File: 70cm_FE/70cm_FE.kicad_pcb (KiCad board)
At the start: 2 copper layers, 60 x 60 mm, 130 parts, among them J2 U.FL, J3 U.FL, J4 U.FL, Q1 2SC3356, Q2 2SC3356, Q3 2SC3356, U1 HT7533-1, U2 74HC14, U3 M68710L, U4 LM393

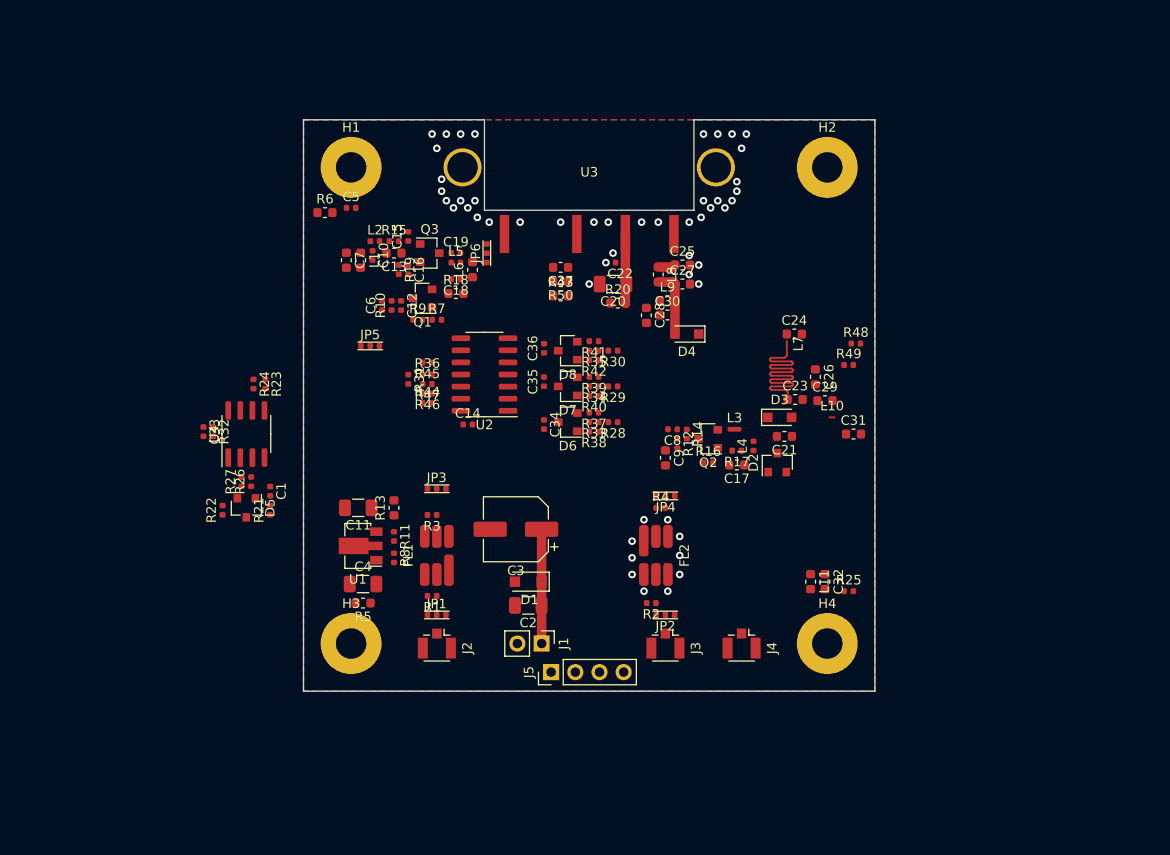
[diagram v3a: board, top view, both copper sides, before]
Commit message: Fix control signal polarities, draft more layout
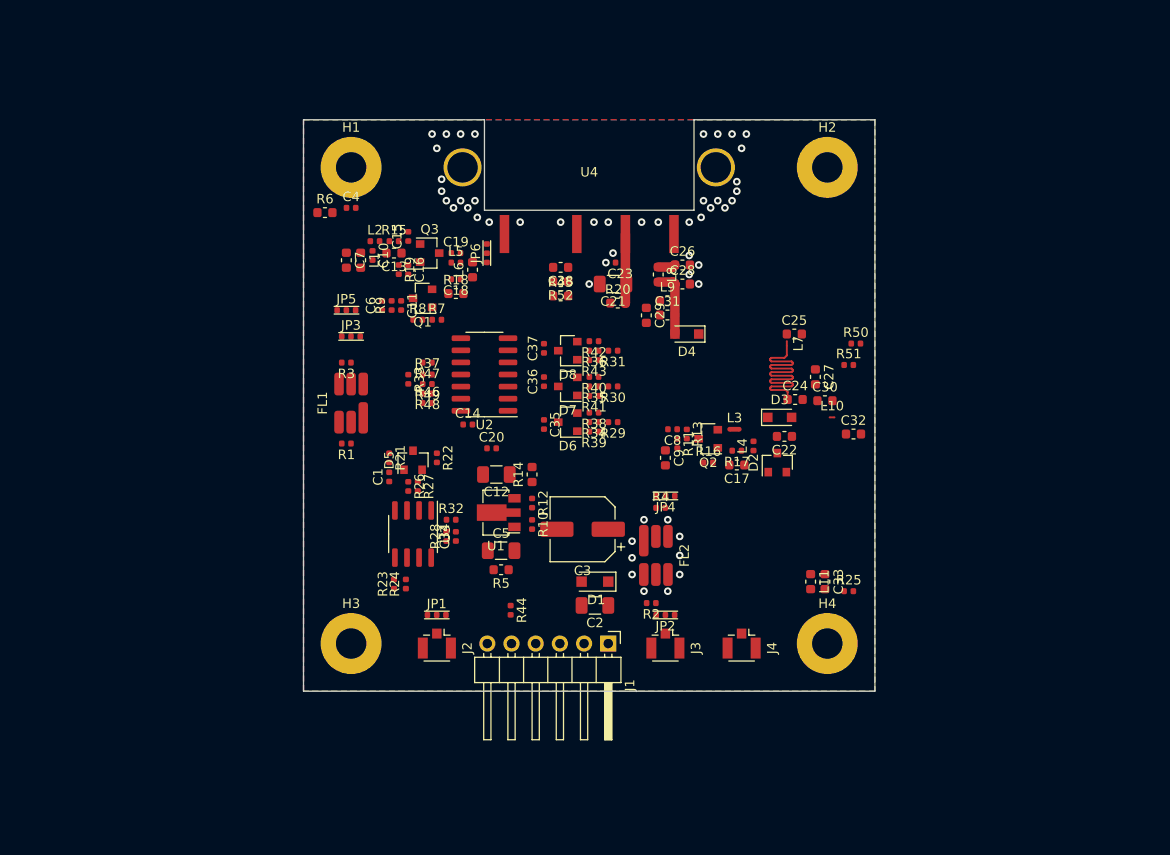
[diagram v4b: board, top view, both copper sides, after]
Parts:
- removed J5: ~, Connector_PinHeader_2.54mm:PinHeader_1x04_P2.54mm_Vertical
- added C20: 100n, Capacitor_SMD:C_0402_1005Metric, F.Cu at (114.8, 84.5)
- added R32: 100, Resistor_SMD:R_0402_1005Metric, F.Cu at (110.5, 92.0)
- added R44: 100, Resistor_SMD:R_0402_1005Metric, F.Cu at (116.8, 101.5)
- J1: footprint Connector_PinHeader_2.54mm:PinHeader_1x02_P2.54mm_Vertical -> Connector_PinHeader_2.54mm:PinHeader_1x06_P2.54mm_Horizontal
- R28: renamed from R32; value 100k -> 220k
- R34: renamed from R33; value 0 -> 220k
- R35: renamed from R34; value 0 -> 100k
- R39: renamed from R38; value DNP -> 0
- moved C34 28.7 mm to (111.0, 93.8), turned to 90 degrees
- moved R28 26.9 mm to (110.0, 93.8), turned to 90 degrees
- moved R24 26.4 mm to (105.8, 98.8), turned to 90 degrees
- moved R23 25.0 mm to (104.5, 98.8), turned to 90 degrees
- moved R22 23.2 mm to (109.0, 85.5), turned to 270 degrees
- moved U3 20.4 mm to (106.5, 93.5), turned to 270 degrees
- moved R27 18.5 mm to (107.0, 88.5), turned to 270 degrees
- moved FL1 18.4 mm to (100.0, 79.8)
- moved JP3 18.4 mm to (99.5, 72.8)
- moved R1 18.4 mm to (99.5, 84.0)
- moved R3 18.4 mm to (99.5, 75.5)
- moved D5 18.2 mm to (106.5, 85.8), turned to 90 degrees
- moved R26 16.5 mm to (106.0, 88.5), turned to 270 degrees
- moved C12 14.9 mm to (115.2, 87.2)
- moved C5 14.9 mm to (115.8, 95.2)
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- renumbered C12 to C11, C11 to C12, C20 to C21, C21 to C22, C22 to C23, C23 to C24, C24 to C25, C25 to C26, C26 to C27, C27 to C28, C28 to C29, C29 to C30, C30 to C31, C31 to C32, C32 to C33, C33 to C34, C34 to C35, C35 to C36, C36 to C37, C37 to C38, C5 to C4, C4 to C5, R8 to R10, R12 to R11, R11 to R12, R14 to R13, R13 to R14, R28 to R29, R29 to R30, R30 to R31, R31 to R33, R35 to R36, R36 to R37, R37 to R38, R39 to R40, R40 to R41, R41 to R42, R42 to R43, R43 to R45, R44 to R46, R45 to R47, R46 to R48, R47 to R49, R48 to R50, R49 to R51, R50 to R52, R9 to R8, R10 to R9, U4 to U3, U3 to U4
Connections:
- net /DET_IN+ renamed /DET_COMP+
- net /DET_IN- renamed /DET_COMP-
- R28 pad 2: /DET_timing -> /DET_COMPout
- R30 pad 1: /TX_ON -> /~TX_ON~
- U2 pad 8: /TX_detect -> /DET_OUT_
- U3 pad 1: /DET_timing -> /DET_COMPout
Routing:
- net /V_in: track 11.5 -> 0.00 mm

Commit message: Add overtemperature protection
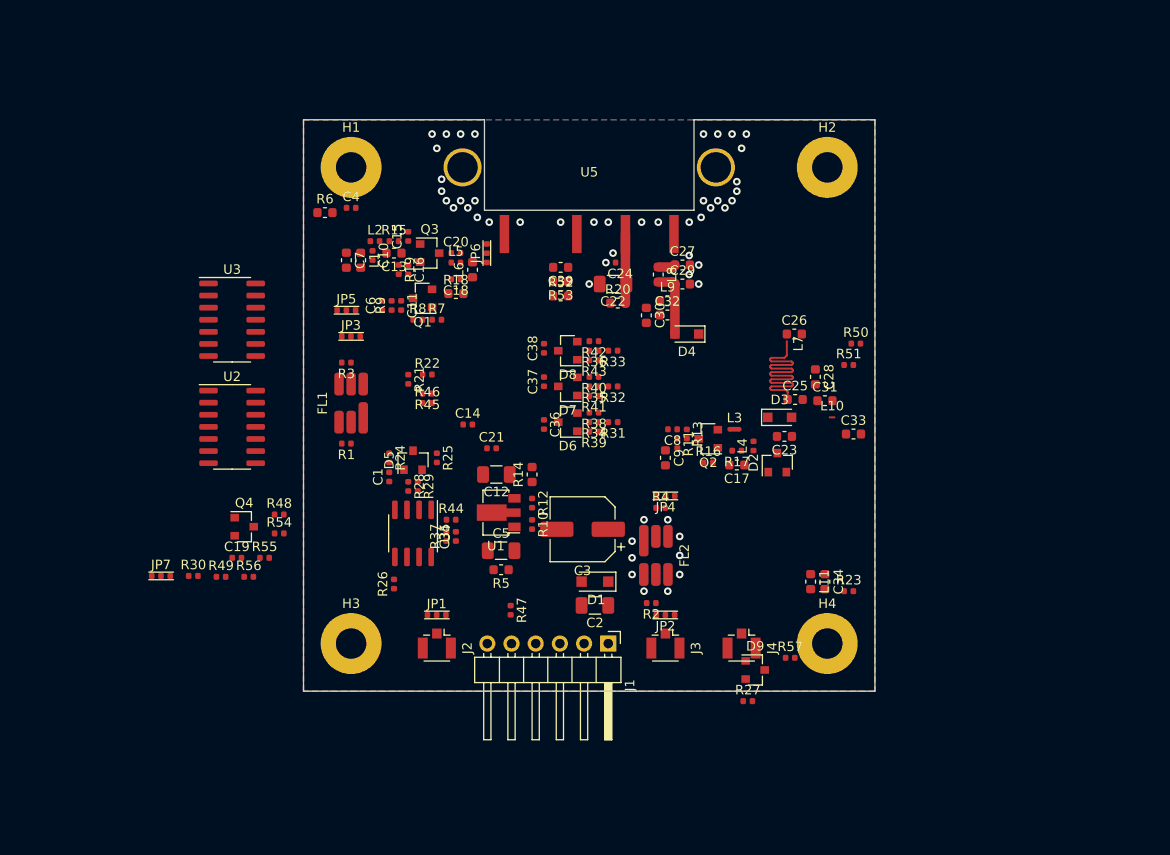
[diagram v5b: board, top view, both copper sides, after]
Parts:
- removed the R24 at (105.8, 98.8)
- removed the R47 at (108.0, 75.5)
- added C19: 100n, Capacitor_SMD:C_0402_1005Metric, F.Cu at (88.0, 96.0)
- added D9: BAV99, Package_TO_SOT_SMD:SOT-23, F.Cu at (142.4, 107.8)
- added JP7: ~, 70cm_FE:Jumper-3_0402, F.Cu at (79.5, 97.9)
- added Q4: 2N7002, Package_TO_SOT_SMD:SOT-23, F.Cu at (88.8, 92.7)
- added R27: 100k, Resistor_SMD:R_0402_1005Metric, F.Cu at (141.7, 111.0)
- added R30: 100k, Resistor_SMD:R_0402_1005Metric, F.Cu at (83.4, 97.9)
- added R48: 100, Resistor_SMD:R_0402_1005Metric, F.Cu at (92.5, 91.5)
- added R54: 1k, Resistor_SMD:R_0402_1005Metric, F.Cu at (92.5, 93.4)
- added R55: 1k, Resistor_SMD:R_0402_1005Metric, F.Cu at (90.9, 96.0)
- added R56: 1k, Resistor_SMD:R_0402_1005Metric, F.Cu at (89.2, 98.0)
- added R57: 10k, Resistor_SMD:R_0402_1005Metric, F.Cu at (146.1, 106.5)
- added U4: LM393, Package_SO:SOIC-8_3.9x4.9mm_P1.27mm, F.Cu at (106.5, 93.4)
- R49: value DNP -> 100k
- U3: value LM393 -> 74HC14; footprint Package_SO:SOIC-8_3.9x4.9mm_P1.27mm -> Package_SO:SOIC-14_3.9x8.7mm_P1.27mm
- moved R49 29.6 mm to (86.3, 98.0), turned to 0 degrees
- moved U3 29.4 mm to (87.5, 71.0), turned to 0 degrees
- moved U2 27.1 mm to (87.5, 82.2), turned to 0 degrees
- renumbered C19 to C20, C20 to C21, C21 to C22, C22 to C23, C23 to C24, C24 to C25, C25 to C26, C26 to C27, C27 to C28, C28 to C29, C29 to C30, C30 to C31, C31 to C32, C32 to C33, C33 to C34, C34 to C35, C35 to C36, C36 to C37, C37 to C38, C38 to C39, R33 to R21, R37 to R22, R25 to R23, R21 to R24, R22 to R25, R23 to R26, R26 to R28, R27 to R29, R29 to R31, R30 to R32, R31 to R33, R28 to R37, R32 to R44, R48 to R45, R44 to R47, R45 to R52, R52 to R53, U4 to U5
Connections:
- R22 pad 2: Net-(R37-Pad2) -> Net-(R22-Pad2)
- R26 pad 1: GND -> /VDD
- R26 pad 2: Net-(R23-Pad2) -> /TempSensor
- R32 pad 1: /~TX_ON~ -> /TX_ON
- R33 pad 1: /~TX_ON~ -> /TX_ON
- R45 pad 1: Net-(R48-Pad1) -> Net-(R45-Pad1)
- R45 pad 2: /TX_ON -> Net-(R45-Pad2)
- R46 pad 1: Net-(R46-Pad1) -> Net-(R45-Pad1)
- R46 pad 2: /~TX_ON~ -> Net-(R46-Pad2)
- R49 pad 1: Net-(R48-Pad1) -> /VDD
- R49 pad 2: /~TX_ON~ -> /~PA_EN_Protected~
- R51 pad 1: Net-(R50-Pad1) -> Net-(R51-Pad1)
- R52 pad 1: /PA_EN -> Net-(R52-Pad1)
- U2 pad 1: /~LNA_EN_SEQ~ -> /~PIN_EN_SEQ~
- U2 pad 10: Net-(R46-Pad1) -> /~PA_EN_1~
- U2 pad 11: Net-(R37-Pad2) -> /~PA_EN_SEQ~
- U2 pad 12: Net-(R48-Pad1) -> Net-(R52-Pad1)
- U2 pad 13: Net-(R46-Pad1) -> /~PA_EN_Protected~
- U2 pad 2: /LNA_EN -> Net-(R45-Pad1)
- U2 pad 3: /~PIN_EN_SEQ~ -> Net-(R45-Pad2)
- U2 pad 5: /~PA_EN_SEQ~ -> Net-(R46-Pad2)
- U2 pad 6: /PA_EN -> Net-(R51-Pad1)
- U2 pad 8: /DET_OUT_ -> /LNA_EN
- U2 pad 9: /DET_timing -> /~LNA_EN_SEQ~
- U3 pad 1: /DET_COMPout -> Net-(R22-Pad2)
- U3 pad 2: /DET_COMP- -> Net-(JP7-Pad3)
- U3 pad 3: /DET_COMP+ -> Net-(JP7-Pad3)
- U3 pad 4: GND -> Net-(JP7-Pad1)
- U3 pad 5: Net-(R23-Pad2) -> /DET_timing
- U3 pad 6: Net-(R24-Pad2) -> /DET_OUT_
- U3 pad 7: Net-(U3-Pad7) -> GND
- U3 pad 8: /VDD -> Net-(U3-Pad8)

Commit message: Change order of inverters for simpler layout
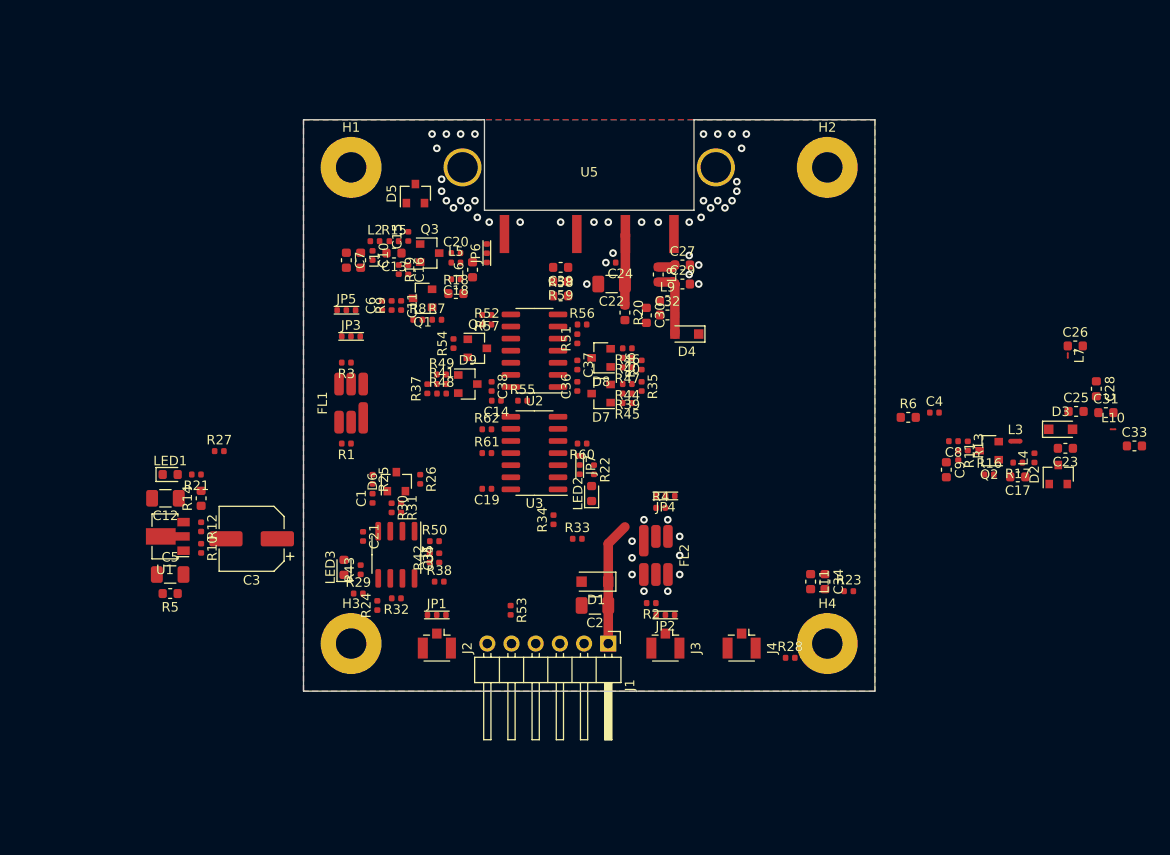
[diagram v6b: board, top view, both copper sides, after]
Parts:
- added LED1: LED, LED_SMD:LED_0603_1608Metric, F.Cu at (81.0, 87.2)
- added LED2: LED, LED_SMD:LED_0603_1608Metric, F.Cu at (125.2, 89.2)
- added LED3: LED, LED_SMD:LED_0603_1608Metric, F.Cu at (99.2, 97.0)
- added R21: 10k, Resistor_SMD:R_0402_1005Metric, F.Cu at (83.8, 87.2)
- added R22: 10k, Resistor_SMD:R_0402_1005Metric, F.Cu at (125.5, 86.8)
- added R29: 1k, Resistor_SMD:R_0402_1005Metric, F.Cu at (100.8, 99.8)
- added R32: 220k, Resistor_SMD:R_0402_1005Metric, F.Cu at (104.8, 100.2)
- added R43: 10k, Resistor_SMD:R_0402_1005Metric, F.Cu at (101.0, 97.2)
- R28: renamed from R57; value 10k -> 22k
- moved C4 64.9 mm to (161.2, 80.8)
- moved R6 64.9 mm to (158.5, 81.2)
- moved D5 61.4 mm to (106.8, 57.8), turned to 90 degrees
- moved R27 61.4 mm to (86.2, 84.8)
- moved JP7 46.1 mm to (124.0, 85.8), turned to 270 degrees
- moved R57 38.4 mm to (114.2, 70.5), turned to 180 degrees
- moved R55 36.7 mm to (118.0, 79.5)
- moved C12 34.8 mm to (80.5, 89.8)
- moved C5 34.8 mm to (81.0, 97.8)
- moved R10 34.8 mm to (84.2, 95.0)
- moved R12 34.8 mm to (84.2, 92.8)
- moved R14 34.8 mm to (84.2, 89.8)
- moved R5 34.8 mm to (81.0, 99.8)
- moved U1 34.8 mm to (80.8, 93.8)
- moved C3 34.8 mm to (89.5, 94.0)
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- renumbered D9 to D5, D5 to D6, D6 to D7, D7 to D8, D8 to D9, R26 to R24, R24 to R25, R25 to R26, R28 to R30, R29 to R31, R21 to R33, R22 to R34, R31 to R35, R32 to R36, R33 to R37, R30 to R38, R34 to R39, R35 to R40, R36 to R41, R37 to R42, R38 to R44, R39 to R45, R40 to R46, R41 to R47, R42 to R48, R43 to R49, R44 to R50, R45 to R51, R46 to R52, R47 to R53, R48 to R54, R49 to R55, R50 to R56, R51 to R57, R52 to R58, R53 to R59, R54 to R60, R55 to R61, R56 to R62
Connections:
- C36 pad 1: /~LNA_EN_SEQ~ -> /~LNA_SEQ_IN~
- C37 pad 1: /~PIN_EN_SEQ~ -> /PIN_SEQ_IN
- C38 pad 1: /~PA_EN_SEQ~ -> /PA_SEQ_IN
- D7 pad 3: /~LNA_EN_SEQ~ -> /~LNA_SEQ_IN~
- D8 pad 3: /~PIN_EN_SEQ~ -> /PIN_SEQ_IN
- D9 pad 3: /~PA_EN_SEQ~ -> /PA_SEQ_IN
- Q4 pad 2: /~PA_EN_1~ -> /~PA_SEQ_OUT~
- Q4 pad 3: /~PA_EN_Protected~ -> /~PA_EN_~
- R39 pad 2: /~LNA_EN_SEQ~ -> /~LNA_SEQ_IN~
- R40 pad 2: /~PIN_EN_SEQ~ -> /PIN_SEQ_IN
- R41 pad 2: /~PA_EN_SEQ~ -> /PA_SEQ_IN
- R51 pad 1: Net-(R45-Pad1) -> /~PIN_SEQ_OUT~
- R51 pad 2: Net-(R45-Pad2) -> /~PIN_EN_~
- R52 pad 1: Net-(R45-Pad1) -> /~PIN_SEQ_OUT~
- R52 pad 2: Net-(R46-Pad2) -> /~DRV_EN_~
- R55 pad 2: /~PA_EN_Protected~ -> /~PA_EN_~
- R56 pad 1: Net-(R50-Pad1) -> /PIN_EN
- R57 pad 1: Net-(R51-Pad1) -> /DRV_EN1
- R58 pad 1: Net-(R52-Pad1) -> /PA_EN
- R60 pad 2: Net-(R54-Pad2) -> Net-(R60-Pad2)
- R62 pad 2: Net-(R56-Pad2) -> Net-(R62-Pad2)
- U2 pad 1: /~PIN_EN_SEQ~ -> /~LNA_SEQ_IN~
- U2 pad 10: /~PA_EN_1~ -> /PA_EN
- U2 pad 11: /~PA_EN_SEQ~ -> /~PA_EN_~
- U2 pad 12: Net-(R52-Pad1) -> /~PA_SEQ_OUT~
- U2 pad 13: /~PA_EN_Protected~ -> /PA_SEQ_IN
- U2 pad 2: Net-(R45-Pad1) -> /LNA_EN
- U2 pad 3: Net-(R45-Pad2) -> /PIN_SEQ_IN
- U2 pad 4: Net-(R50-Pad1) -> /~PIN_SEQ_OUT~
- U2 pad 5: Net-(R46-Pad2) -> /~PIN_EN_~
- U2 pad 6: Net-(R51-Pad1) -> /PIN_EN
- U2 pad 8: /LNA_EN -> /DRV_EN1
- U2 pad 9: /~LNA_EN_SEQ~ -> /~DRV_EN_~
- U3 pad 12: Net-(U3-Pad12) -> /DET_OUT_
- U3 pad 13: Net-(R56-Pad2) -> /DET_timing
- U3 pad 5: /DET_timing -> Net-(R60-Pad2)
- U3 pad 6: /DET_OUT_ -> Net-(U3-Pad6)
- U3 pad 9: Net-(R54-Pad2) -> Net-(R62-Pad2)
- U4 pad 5: /TempSensor -> /TempHysteresis
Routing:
- net /PIN_RXRF: track 26.6 -> 0.00 mm
- net /V_in: track 0.00 -> 13.0 mm
- net /PA_VDD: track 7.26 -> 7.78 mm

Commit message: Change PCB size to 50x70 mm, place some components
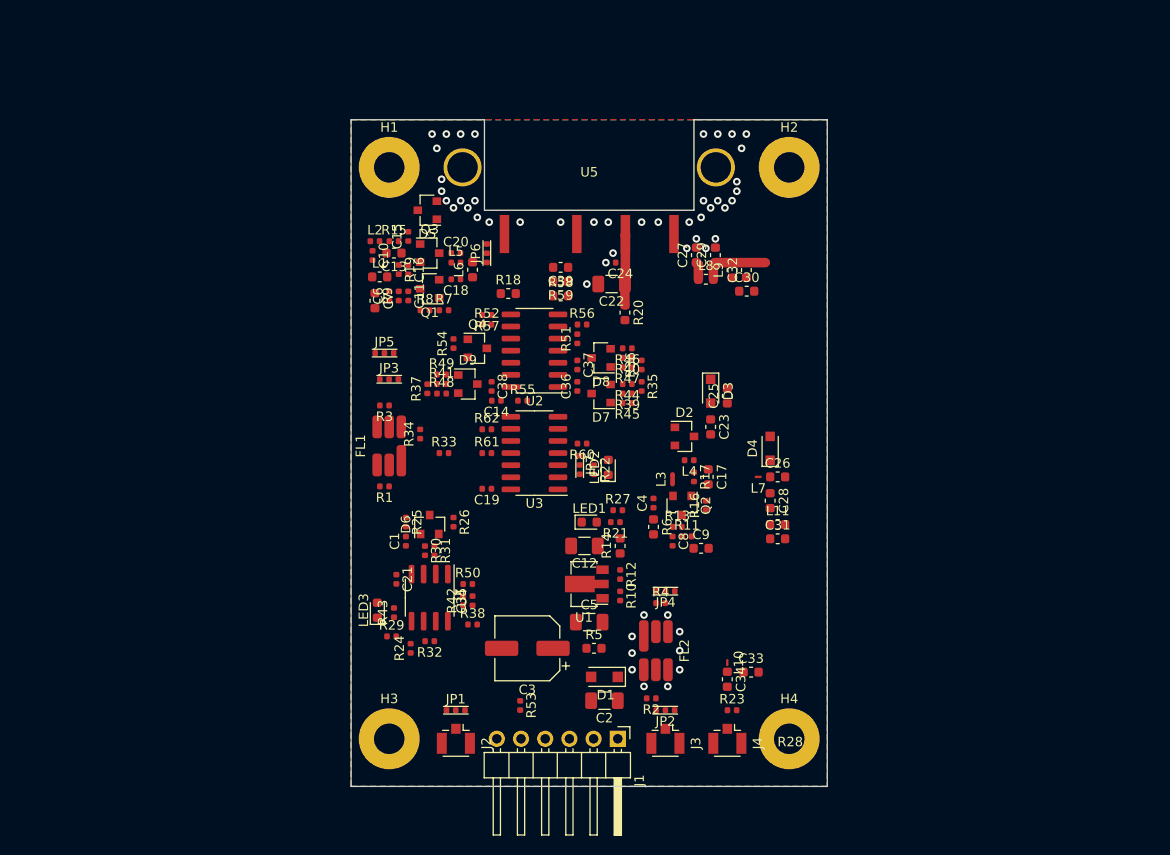
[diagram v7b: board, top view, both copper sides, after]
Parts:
- C25, C26: value 5p6 -> 4p7
- C28: value C -> 33p
- C31, C33: value C -> 10p
- C34: value C -> 100p
- L10: value L -> 23 mm; footprint 70cm_FE:NetTie-2_SMD_Pad0.2mm -> 70cm_FE:NetTie-2_SMD_Pad0.25mm
- L11: value L -> 68n
- L7: value 15n -> 24 mm; footprint 70cm_FE:NetTie-2_SMD_Pad0.2mm -> 70cm_FE:NetTie-2_SMD_Pad0.25mm
- moved L10 47.3 mm to (139.5, 107.0), turned to 270 degrees
- moved C33 46.7 mm to (142.0, 108.0)
- moved R5 44.9 mm to (125.5, 105.5), turned to 0 degrees
- moved C12 44.3 mm to (124.5, 94.8)
- moved C5 44.3 mm to (125.0, 102.8)
- moved LED1 44.3 mm to (125.0, 92.2)
- moved R10 44.3 mm to (128.2, 100.0)
- moved R12 44.3 mm to (128.2, 97.8)
- moved R14 44.3 mm to (128.2, 94.8)
- moved R21 44.3 mm to (127.8, 92.2)
- moved U1 44.3 mm to (124.8, 98.8)
- moved R27 42.3 mm to (128.0, 91.0)
- moved D2 39.5 mm to (135.0, 83.2), turned to 0 degrees
- moved C23 37.3 mm to (137.8, 82.2), turned to 270 degrees
- moved D3 37.0 mm to (137.8, 78.5), turned to 270 degrees
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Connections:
- L11 pad 1: Net-(C33-Pad1) -> Net-(C28-Pad2)
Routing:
- net /V_in: track 13.0 -> 0.00 mm
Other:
- board size 60 x 60 mm -> 50 x 70 mm
